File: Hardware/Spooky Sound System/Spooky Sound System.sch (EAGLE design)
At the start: 18 parts, among them U1 LM3886TF/NOPB, U2 LM3886TF/NOPB, U3 LM3886TF/NOPB

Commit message: tone control done.
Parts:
- added C10, C17: 220nF, MF_Passives:CAPACITOR_NP_0805
- added C11, C18: 47uF, MF_Passives:CAPACITOR_P_6.3MM
- added C12, C13, C19: 10uF, MF_Passives:CAPACITOR_P_4MM
- added C14, C7: 2.2nF, MF_Passives:CAPACITOR_NP_0805
- added C15, C16, C8, C9: 22nF, MF_Passives:CAPACITOR_NP_0805
- added P1, P2, P3: 100K, PP_Passives:DUAL_TAPER_POTENTIOMETER
- added R10: 12K, MF_Passives:RESISTOR_0805
- added R11, R12: 100K, MF_Passives:RESISTOR_0805
- C1, C3, C5: value 47uF -> 0.1uF; device MF_Passives:CAPACITOR_NP_0805 -> MF_Passives:CAPACITOR_NP_1206; MPN (none) -> VJ1206Y104JXBTW1BC
- C2, C4: value 100uF -> 0.1uF; device MF_Passives:CAPACITOR_P_6.3MM -> MF_Passives:CAPACITOR_NP_1206; MPN (none) -> VJ1206Y104JXBTW1BC
- C6: value 100uF -> 10uF; device MF_Passives:CAPACITOR_P_6.3MM -> MF_Passives:CAPACITOR_P_4MM; MPN (none) -> MF-CAP-4MM-10uF
- R1, R7: value 1K -> 10K
- R2, R8: value 22K -> 10K
- R3, R9: value 22K -> 4.7K
- R4: value 1K -> 12K
- R5, R6: value 22K -> 100K
- U1: value LM3886TF/NOPB -> TDA7387; device PP_AnalogIC:LM3886 -> PP_AnalogIC:TDA7387; MPN LM3886TF/NOPB -> (none)
- U2, U3: value LM3886TF/NOPB -> AZ4558C; device PP_AnalogIC:LM3886 -> PP_AnalogIC:AZ4558C; MPN LM3886TF/NOPB -> (none)
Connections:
- removed net V+: C2.P$1, C4.P$1, C6.P$1, U1.1,5, U2.1,5, U3.1,5
- new net AC-GND: C5.P$2, U1.AC-GND
- new net IN_L: U2_A.INPUT_1+
- new net IN_R: U3_A.INPUT_1+
- new net N$11: C11.P$1, R5.P$2, R6.P$1, U2_B.INPUT_2+
- new net N$12: C13.P$2, U3_A.INPUT_1-, U3_A.OUTPUT_1
- new net N$13: C13.P$1, C14.P$1, R7.P$1
- new net N$14: C16.P$1, P1_B.1, R7.P$2
- new net N$15: C16.P$2, C17.P$1, P1_B.2, R8.P$2
- new net N$16: C17.P$2, P1_B.3, R10.P$2
- new net N$17: R8.P$1, R9.P$2, U3_B.INPUT_2-
- new net N$18: P2_B.2, R9.P$1
- new net N$19: C14.P$2, P2_B.1
- new net N$20: C15.P$1, P2_B.3
- new net N$21: C15.P$2, C19.P$1, R10.P$1, U3_B.OUTPUT_2
- new net N$22: C18.P$1, R11.P$2, R12.P$1, U3_B.INPUT_2+
- new net OUT_L: C12.P$2, P3_A.3
- new net OUT_R: C19.P$2, P3_B.1
- new net TDA7387_IN1: C1.P$2, U1.IN1
- new net TDA7387_IN2: C2.P$2, U1.IN2
- new net TDA7387_IN3: C3.P$2, U1.IN3
- new net TDA7387_IN4: C4.P$2, U1.IN4
- new net VIN: R11.P$1, R5.P$1, U2_A.VCC, U3_A.VCC
- net GND: now also C11.P$2, C18.P$2, P3_A.1, P3_B.3, R12.P$2, R6.P$2, U2_A.VEE, U3_A.VEE; no longer C1.P$2, C2.P$2, C3.P$2, C4.P$2, C5.P$2, C6.P$2, R2.P$2, R5.P$2, R8.P$2, U1.7, U1.8, U2.7, U2.8, U3.7, U3.8
- net N$1: now also C6.P$2, U2_A.INPUT_1-, U2_A.OUTPUT_1; no longer R1.P$2, R2.P$1, U1.10
- net N$10: now also C12.P$1, C8.P$2, R4.P$1, U2_B.OUTPUT_2; no longer C5.P$1, R9.P$2
- net N$2: now also C6.P$1, C7.P$1; no longer R4.P$1, R7.P$1
- net N$3: now also C9.P$1, P1_A.1, R1.P$2; no longer R3.P$1, U1.9
- net N$4: now also C10.P$1, C9.P$2, P1_A.2, R2.P$2; no longer C1.P$1, R3.P$2
- net N$5: now also C10.P$2, P1_A.3; no longer R5.P$1, U2.10
- net N$6: now also R2.P$1, R3.P$2, U2_B.INPUT_2-; no longer R6.P$1, U2.9
- net N$7: now also P2_A.2, R3.P$1; no longer C3.P$1, R6.P$2
- net N$8: now also C7.P$2, P2_A.1; no longer R7.P$2, R8.P$1, U3.10
- net N$9: now also C8.P$1, P2_A.3; no longer R9.P$1, U3.9
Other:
- moved on the sheet: C1, C3, C5, C6, R1, R2, R3, R4, R5, R6, R7, R8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

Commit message: Schematic done. Start Routing.
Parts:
- added C20, C21, C22, C23: 0.01uF, MF_Passives:CAPACITOR_NP_1210
- added C24: 22nF, MF_Passives:CAPACITOR_NP_0805
- added C25, C27, C28, C31: 10uF, MF_Passives:CAPACITOR_P_4MM
- added C26: 0.1uF, MF_Passives:CAPACITOR_NP_0805
- added C29, C30: 1000uF, MF_Passives:CAPACITOR_P_12.5MM
- added C32: 47uF, MF_Passives:CAPACITOR_P_6.3MM
- added C33, C34, C35: 100uF, MF_Passives:CAPACITOR_P_6.3MM
- added J1: SJ1-3533NS, PP_Connectors:TRS_SHIELD_JACK_SJ1-3533NS
- added J2, J3, J4: 1546215-2, PP_Connectors:CON_01X02_1546215-2
- added P4, P5: 100K, PP_Passives:DUAL_TAPER_POTENTIOMETER
- added R13, R14, R19, R20: 1M, MF_Passives:RESISTOR_0805
- added R15, R16, R17, R18, R21, R22, R23, R24, R27, R30, R31, R32: 0, MF_Passives:RESISTOR_0805
- added R25, R26, R28, R29: 10K, MF_Passives:RESISTOR_0805
- added R33, R34: 220K, MF_Passives:RESISTOR_0805
- added R35: 1K, MF_Passives:RESISTOR_0805
- added U4, U5, U6: AZ4558C, PP_AnalogIC:AZ4558C
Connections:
- new net AUD_IN_L: C20.P$1, C22.P$1, J1.T
- new net AUD_IN_R: C21.P$1, C23.P$1, J1.R
- new net L+: J2.PIN1, U1.OUT1+
- new net L-: J2.PIN2, U1.OUT1-
- new net N$23: C27.P$2, R21.P$2, U4_A.OUTPUT_1
- new net N$24: P5_A.3, R21.P$1
- new net N$25: P3_B.3, R16.P$1
- new net N$26: P3_B.1, R17.P$2
- new net N$27: C28.P$2, R23.P$2, U4_B.OUTPUT_2
- new net N$28: P5_B.3, R23.P$1
- new net N$29: C26.P$1, R25.P$2, R26.P$2, R28.P$1, U5_A.INPUT_1-
- new net N$30: C26.P$2, P4_A.3, R28.P$2, U5_A.OUTPUT_1
- new net N$31: R29.P$1, U5_A.INPUT_1+
- new net N$32: P4_A.2, R31.P$2
- new net N$33: R30.P$2, R32.P$1, U5_B.INPUT_2-
- new net N$34: C25.P$1, R30.P$1, U5_B.OUTPUT_2
- new net N$35: P5_A.2, U4_A.INPUT_1-
- new net N$36: P5_A.1, R22.P$2
- new net N$37: P5_B.1, R24.P$2
- new net N$38: P5_B.2, U4_B.INPUT_2-
- new net N$39: P3_B.2, U3_A.INPUT_1-
- new net N$40: P3_A.3, R18.P$2
- new net N$41: P3_A.2, U2_A.INPUT_1-
- new net N$42: P3_A.1, R15.P$1
- new net N$43: C24.P$1, R31.P$1, U5_B.INPUT_2+
- new net N$44: C25.P$2, R27.P$1
- new net N$45: C27.P$1, R26.P$1
- new net N$46: C28.P$1, R25.P$1
- new net N$47: C33.P$2, C34.P$1, R33.P$2, R34.P$1, U6_A.INPUT_1+
- new net N$48: R35.P$1, U6_A.OUTPUT_1
- new net N$49: C32.P$1, U1.SVR
- new net OUT_SUB: C3.P$1, R27.P$2
- new net R+: J3.PIN1, U1.OUT2+
- new net R-: J3.PIN2, U1.OUT2-
- new net SUB+: J4.PIN1, U1.OUT3+
- new net SUB-: J4.PIN2, U1.OUT3-
- new net SUB_L: C22.P$2, R19.P$1
- new net SUB_R: C23.P$2, R20.P$1, U4_B.INPUT_2+
- new net VGND: C11.P$2, C18.P$2, C24.P$2, R12.P$2, R13.P$2, R14.P$2, R17.P$1, R18.P$1, R19.P$2, R20.P$2, R22.P$1, R24.P$1, R29.P$2, R32.P$2, R35.P$2, R6.P$2, U6_A.INPUT_1-
- net GND: now also C29.P$2, C30.P$2, C31.P$2, C32.P$2, C34.P$2, C35.P$2, C4.P$1, C5.P$1, J1.S, J1.SHIELD, R34.P$2, U1.PW-GND1, U1.PW-GND2, U1.PW-GND3, U1.PW-GND4, U1.S-GND, U1.TAB, U4_A.VEE, U5_A.VEE, U6_A.VEE; no longer C11.P$2, C18.P$2, P3_A.1, P3_B.3, R12.P$2, R6.P$2
- net IN_L: now also C20.P$2, R14.P$1
- net IN_R: now also C21.P$2, R13.P$1
- net N$1: now also R15.P$2; no longer U2_A.INPUT_1-
- net N$12: now also R16.P$2; no longer U3_A.INPUT_1-
- net OUT_L: now also C1.P$1; no longer P3_A.3
- net OUT_R: now also C2.P$1; no longer P3_B.1
- net VIN: now also C29.P$1, C30.P$1, C31.P$1, C33.P$1, C35.P$1, R33.P$1, U1.MUTE, U1.ST-BY, U1.VCC_1-2, U1.VCC_3-4, U4_A.VCC, U5_A.VCC, U6_A.VCC
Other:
- moved on the sheet: C1, C2, C3, C4, C5, P3_A, P3_B, U1

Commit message: Starting layout...
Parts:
- added J5: 1546215-2, PP_Connectors:CON_01X02_1546215-2
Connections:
- net GND: now also J5.PIN2
- net VIN: now also J5.PIN1
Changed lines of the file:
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@@
 <grid distance="0.1" unitdist="inch" unit="inch" style="lines" multiple="1" display="no" altdistance="0.01" altunitdist="inch" altunit="inch"/>
 <layers>
-<layer number="1" name="Top" color="4" fill="1" visible="yes" active="no"/>
-<layer number="2" name="Route2" color="1" fill="3" visible="yes" active="no"/>
-<layer number="3" name="Route3" color="4" fill="3" visible="yes" active="no"/>
-<layer number="4" name="Route4" color="1" fill="4" visible="yes" active="no"/>
-<layer number="5" name="Route5" color="4" fill="4" visible="yes" active="no"/>
-<layer number="6" name="Route6" color="1" fill="8" visible="yes" active="no"/>
-<layer number="7" name="Route7" color="4" fill="8" visible="yes" active="no"/>
-<layer number="8" name="Route8" color="1" fill="2" visible="yes" active="no"/>
-<layer number="9" name="Route9" color="4" fill="2" visible="yes" active="no"/>
-<layer number="10" name="Route10" color="1" fill="7" visible="yes" active="no"/>
-<layer number="11" name="Route11" color="4" fill="7" visible="yes" active="no"/>
-<layer number="12" name="Route12" color="1" fill="5" visible="yes" active="no"/>
-<layer number="13" name="Route13" color="4" fill="5" visible="yes" active="no"/>
-<layer number="14" name="Route14" color="1" fill="6" visible="yes" active="no"/>
-<layer number="15" name="Route15" color="4" fill="6" visible="yes" active="no"/>
-<layer number="16" name="Bottom" color="1" fill="1" visible="yes" active="no"/>
-<layer number="17" name="Pads" color="2" fill="1" visible="yes" active="no"/>
-<layer number="18" name="Vias" color="2" fill="1" visible="yes" active="no"/>
-<layer number="19" name="Unrouted" color="6" fill="1" visible="yes" active="no"/>
-<layer number="20" name="Dimension" color="15" fill="1" visible="yes" active="no"/>
-<layer number="21" name="tPlace" color="7" fill="1" visible="yes" active="no"/>
-<layer number="22" name="bPlace" color="7" fill="1" visible="yes" active="no"/>
-<layer number="23" name="tOrigins" color="15" fill="1" visible="yes" active="no"/>
-<layer number="24" name="bOrigins" color="15" fill="1" visible="yes" active="no"/>
-<layer number="25" name="tNames" color="7" fill="1" visible="yes" active="no"/>
-<layer number="26" name="bNames" color="7" fill="1" visible="yes" active="no"/>
-<layer number="27" name="tValues" color="7" fill="1" visible="yes" active="no"/>
-<layer number="28" name="bValues" color="7" fill="1" visible="yes" active="no"/>
+<layer number="1" name="Top" color="4" fill="1" visible="no" active="no"/>
+<layer number="2" name="Route2" color="1" fill="3" visible="no" active="no"/>
+<layer number="3" name="Route3" color="4" fill="3" visible="no" active="no"/>
+<layer number="4" name="Route4" color="1" fill="4" visible="no" active="no"/>
+<layer number="5" name="Route5" color="4" fill="4" visible="no" active="no"/>
+<layer number="6" name="Route6" color="1" fill="8" visible="no" active="no"/>
+<layer number="7" name="Route7" color="4" fill="8" visible="no" active="no"/>
+<layer number="8" name="Route8" color="1" fill="2" visible="no" active="no"/>
+<layer number="9" name="Route9" color="4" fill="2" visible="no" active="no"/>
+<layer number="10" name="Route10" color="1" fill="7" visible="no" active="no"/>
+<layer number="11" name="Route11" color="4" fill="7" visible="no" active="no"/>
+<layer number="12" name="Route12" color="1" fill="5" visible="no" active="no"/>
+<layer number="13" name="Route13" color="4" fill="5" visible="no" active="no"/>
+<layer number="14" name="Route14" color="1" fill="6" visible="no" active="no"/>
+<layer number="15" name="Route15" color="4" fill="6" visible="no" active="no"/>
+<layer number="16" name="Bottom" color="1" fill="1" visible="no" active="no"/>
+<layer number="17" name="Pads" color="2" fill="1" visible="no" active="no"/>
+<layer number="18" name="Vias" color="2" fill="1" visible="no" active="no"/>
+<layer number="19" name="Unrouted" color="6" fill="1" visible="no" active="no"/>
+<layer number="20" name="Dimension" color="15" fill="1" visible="no" active="no"/>
+<layer number="21" name="tPlace" color="7" fill="1" visible="no" active="no"/>
+<layer number="22" name="bPlace" color="7" fill="1" visible="no" active="no"/>
+<layer number="23" name="tOrigins" color="15" fill="1" visible="no" active="no"/>
+<layer number="24" name="bOrigins" color="15" fill="1" visible="no" active="no"/>
+<layer number="25" name="tNames" color="7" fill="1" visible="no" active="no"/>
+<layer number="26" name="bNames" color="7" fill="1" visible="no" active="no"/>
+<layer number="27" name="tValues" color="7" fill="1" visible="no" active="no"/>
+<layer number="28" name="bValues" color="7" fill="1" visible="no" active="no"/>
 <layer number="29" name="tStop" color="7" fill="3" visible="no" active="no"/>
 <layer number="30" name="bStop" color="7" fill="6" visible="no" active="no"/>
@@
 <layer number="35" name="tGlue" color="7" fill="4" visible="no" active="no"/>
 <layer number="36" name="bGlue" color="7" fill="5" visible="no" active="no"/>
-<layer number="37" name="tTest" color="7" fill="1" visible="yes" active="no"/>
-<layer number="38" name="bTest" color="7" fill="1" visible="yes" active="no"/>
+<layer number="37" name="tTest" color="7" fill="1" visible="no" active="no"/>
+<layer number="38" name="bTest" color="7" fill="1" visible="no" active="no"/>
 <layer number="39" name="tKeepout" color="4" fill="11" visible="no" active="no"/>
 <layer number="40" name="bKeepout" color="1" fill="11" visible="no" active="no"/>
@@
 <layer number="44" name="Drills" color="7" fill="1" visible="no" active="no"/>
 <layer number="45" name="Holes" color="7" fill="1" visible="no" active="no"/>
-<layer number="46" name="Milling" color="3" fill="1" visible="yes" active="no"/>
-<layer number="47" name="Measures" color="7" fill="1" visible="yes" active="no"/>
-<layer number="48" name="Document" color="7" fill="1" visible="yes" active="no"/>
-<layer number="49" name="Reference" color="7" fill="1" visible="yes" active="no"/>
-<layer number="50" name="dxf" color="7" fill="1" visible="yes" active="no"/>
-<layer number="51" name="tDocu" color="7" fill="1" visible="yes" active="no"/>
-<layer number="52" name="bDocu" color="7" fill="1" visible="yes" active="no"/>
-<layer number="53" name="tGND_GNDA" color="7" fill="9" visible="yes" active="no"/>
-<layer number="54" name="bGND_GNDA" color="1" fill="9" visible="yes" active="no"/>
-<layer number="56" name="wert" color="7" fill="1" visible="yes" active="no"/>
+<layer number="46" name="Milling" color="3" fill="1" visible="no" active="no"/>
+<layer number="47" name="Measures" color="7" fill="1" visible="no" active="no"/>
+<layer number="48" name="Document" color="7" fill="1" visible="no" active="no"/>
+<layer number="49" name="Reference" color="7" fill="1" visible="no" active="no"/>
+<layer number="50" name="dxf" color="7" fill="1" visible="no" active="no"/>
+<layer number="51" name="tDocu" color="7" fill="1" visible="no" active="no"/>
+<layer number="52" name="bDocu" color="7" fill="1" visible="no" active="no"/>
+<layer number="53" name="tGND_GNDA" color="7" fill="9" visible="no" active="no"/>
+<layer number="54" name="bGND_GNDA" color="1" fill="9" visible="no" active="no"/>
+<layer number="56" name="wert" color="7" fill="1" visible="no" active="no"/>
 <layer number="90" name="Modules" color="5" fill="1" visible="yes" active="yes"/>
 <layer number="91" name="Nets" color="2" fill="1" visible="yes" active="yes"/>
@@
 <part name="U$11" library="MF_Aesthetics" deviceset="POWER_RAIL" device="" value="VIN"/>
 <part name="U$12" library="MF_Aesthetics" deviceset="GND_RAIL" device="" value="GND"/>
-<part name="U$13" library="MF_Aesthetics" deviceset="GND_RAIL" device="" value="GND"/>
+<part name="U$13" library="MF_Aesthetics" deviceset="GND_RAIL" device="" value="VGND"/>
 <part name="C30" library="MF_Passives" deviceset="CAPACITOR_P" device="_12.5MM" value="1000uF">
 <attribute name="MPN" value="MF-CAP-12.5MM-1000uF"/>
@@
 <attribute name="LABEL01" value="SUB+"/>
 <attribute name="LABEL02" value="SUB-"/>
+</part>
+<part name="J5" library="PP_Connectors" deviceset="CON_01X02" device="_1546215-2" value="1546215-2">
+<attribute name="LABEL01" value="VIN"/>
+<attribute name="LABEL02" value="GND"/>
 </part>
 </parts>
@@
 <instance part="J3" gate="G$1" x="30.48" y="172.72"/>
 <instance part="J4" gate="G$1" x="30.48" y="154.94"/>
+<instance part="J5" gate="G$1" x="-271.78" y="236.22" rot="MR0"/>
 </instances>
 <busses>
@@
 <wire x1="-83.82" y1="193.04" x2="-83.82" y2="190.5" width="0.1524" layer="91"/>
 <junction x="-83.82" y="190.5"/>
+</segment>
+<segment>
+<pinref part="J5" gate="G$1" pin="PIN1"/>
+<wire x1="-269.24" y1="236.22" x2="-261.62" y2="236.22" width="0.1524" layer="91"/>
+<label x="-266.7" y="236.22" size="1.016" layer="95" font="vector"/>
 </segment>
 </net>
@@
 <wire x1="-203.2" y1="160.02" x2="-203.2" y2="154.94" width="0.1524" layer="91"/>
 <junction x="-203.2" y="160.02"/>
+<label x="-210.82" y="160.02" size="1.27" layer="95" font="vector"/>
 </segment>
 </net>
@@
 <junction x="7.62" y="144.78"/>
 <junction x="7.62" y="127"/>
+<junction x="-63.5" y="121.92"/>
 </segment>
 <segment>
@@
 <label x="-271.78" y="215.9" size="1.016" layer="95" font="vector"/>
 </segment>
-</net>
+<segment>
+<pinref part="J5" gate="G$1" pin="PIN2"/>
+<wire x1="-269.24" y1="233.68" x2="-261.62" y2="233.68" width="0.1524" layer="91"/>
+<label x="-266.7" y="233.68" size="1.016" layer="95" font="vector"/>
+</segment>
+</net>

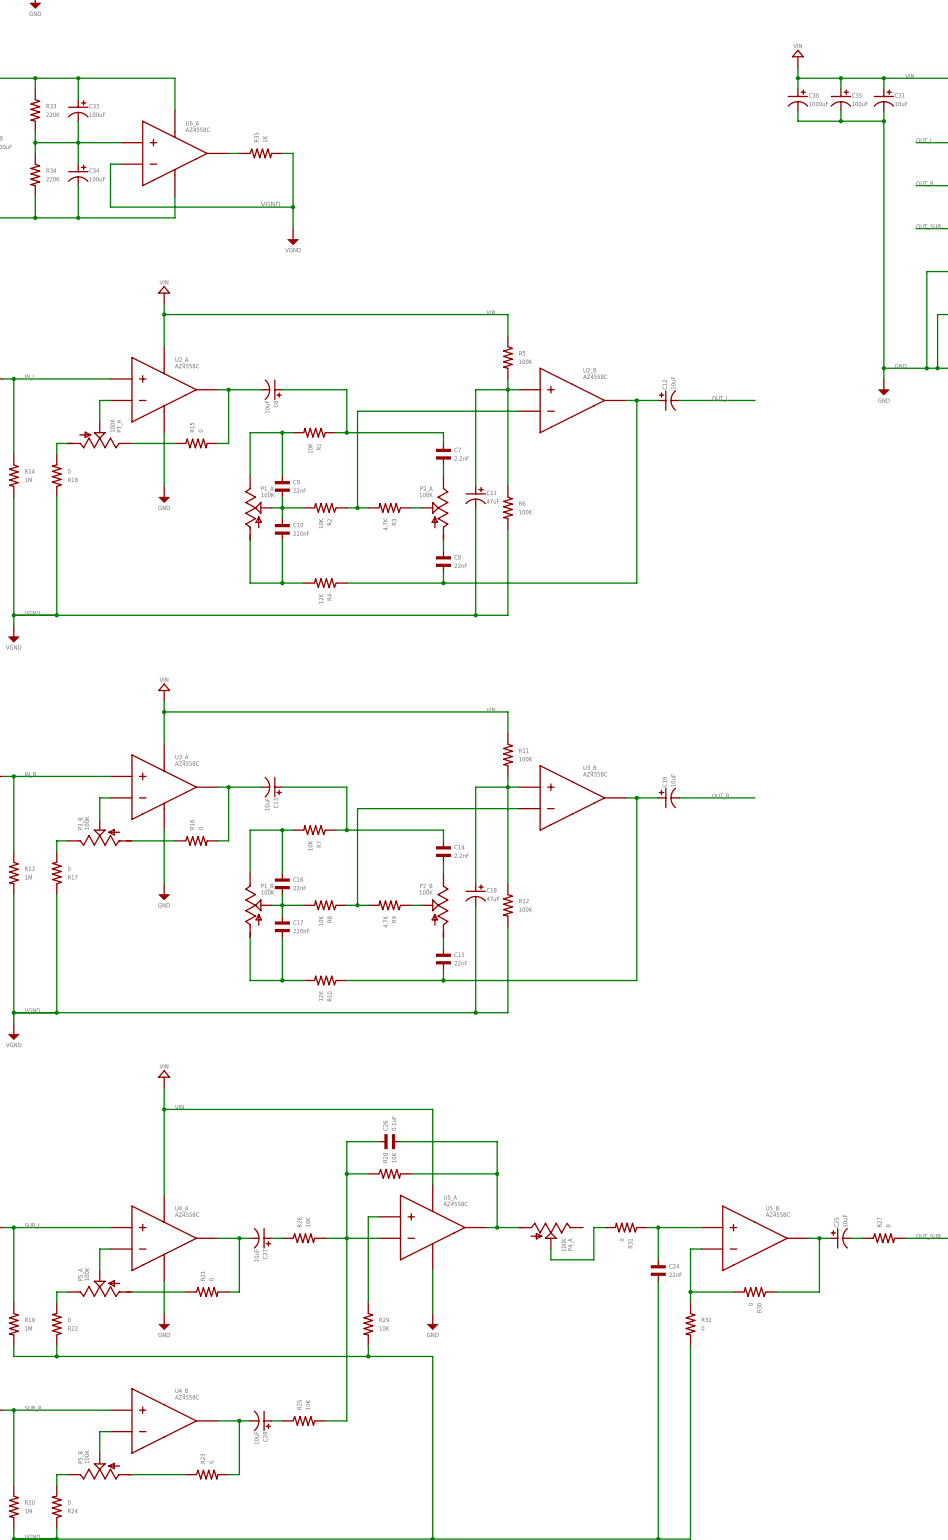
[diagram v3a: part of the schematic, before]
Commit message: Parts layed out
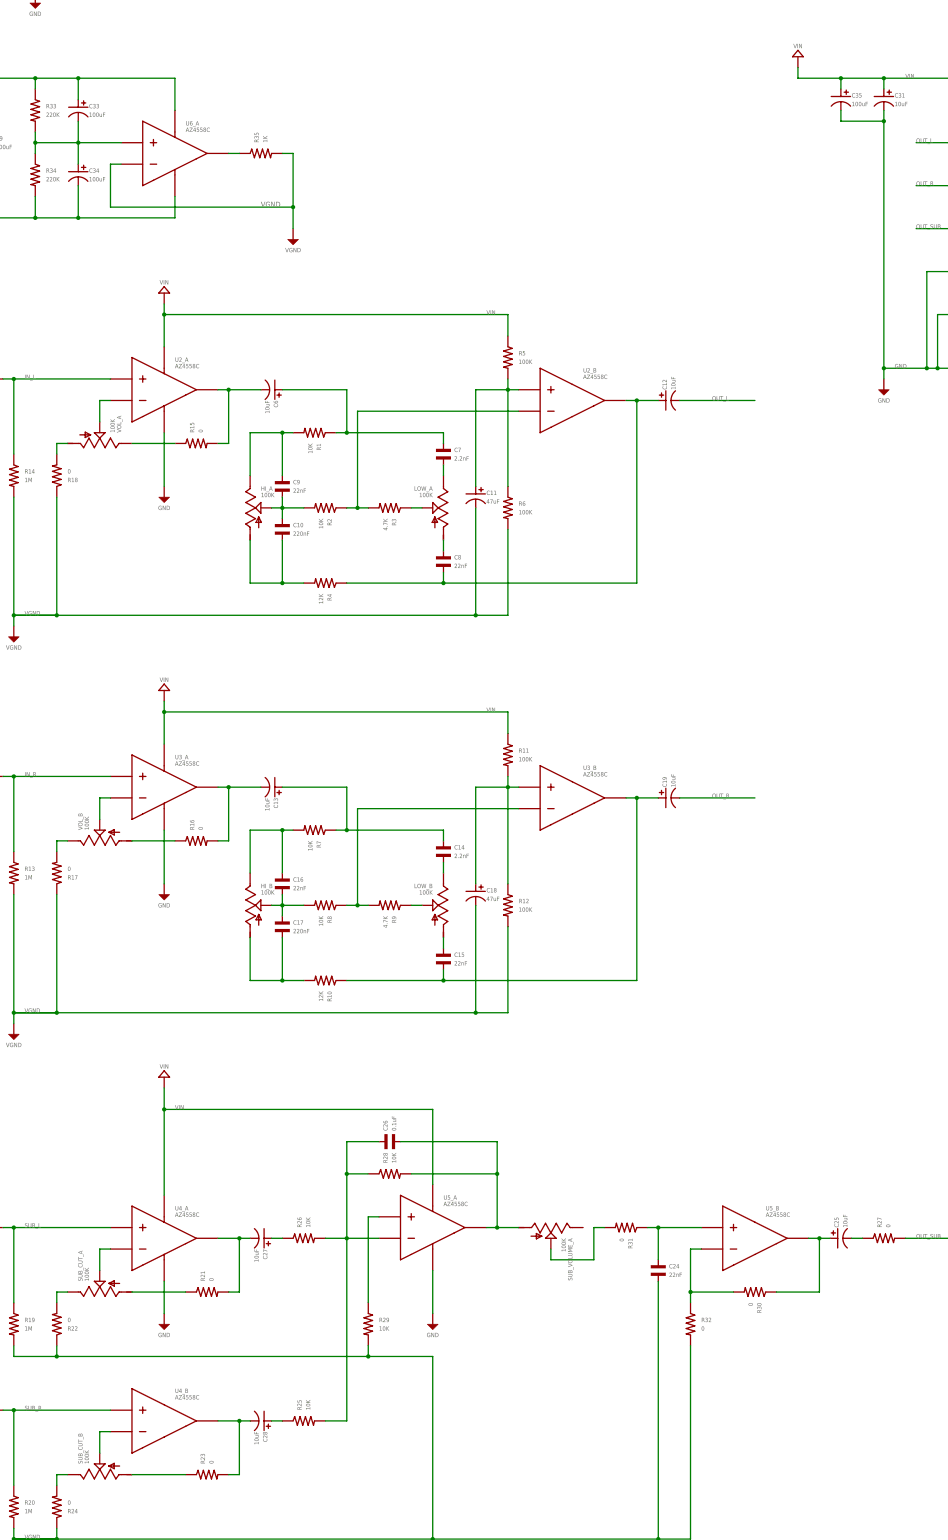
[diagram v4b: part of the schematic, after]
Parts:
- removed C30: 1000uF, MF_Passives:CAPACITOR_P_12.5MM
- renumbered P1 to HI, P2 to LOW, P3 to VOL, P4 to SUB_VOLUME, P5 to SUB_CUT
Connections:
- net GND: no longer C30.P$2
- net SUB_L: now also U4_A.INPUT_1+
- net VIN: no longer C30.P$1
